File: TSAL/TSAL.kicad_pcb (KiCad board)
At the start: 2 copper layers, 100 x 56 mm, 129 parts, among them IC1 ISO224ADWVR, IC2 ISO224ADWVR, IC3 LTC6995IS6-2#TRMPBF, IC4 LTC6995IS6-2#TRMPBF, J1 Conn_SDC, J2 Conn_TSAL, J3 Conn_AIR, J4 Conn_01x02, J5 Conn_VI, J6 Conn_Control, J7 Conn_HV, J8 Conn_Pre, K1 G2RL-2, Q1 ZXM61N02F, Q2 ZXM61N02F, Q3 ZXM61N02F, Q4 ZXM61N02F, Q5 IXTA6N100D2, U3 TLV7041DBV, U4 TLV7041DBV, U5 74LVC1G08, U6 AP2205-W5-7, U7 AP2205-W5-7, U9 AP2204K-ADJ

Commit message: chore: basic section of layout
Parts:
- removed C11, C13, C18: 0.1u, Capacitor_SMD:C_0603_1608Metric
- removed C12: 0.22u, Capacitor_SMD:C_0603_1608Metric
- removed C14, C15, C19, C33: 1u, Capacitor_SMD:C_0603_1608Metric
- removed IC1, IC2: ISO224ADWVR, Package_SO:SOIC-8_7.5x5.85mm_P1.27mm
- removed RV2, RV4: 10K, Potentiometer_THT:Potentiometer_Bourns_3296W_Vertical
- removed TP3, TP9: TestPoint, TestPoint:TestPoint_THTPad_D1.5mm_Drill0.7mm
- added C1: 330p, Capacitor_SMD:C_0603_1608Metric, F.Cu at (111.0, 104.3)
- added C3: 330p, Capacitor_SMD:C_0603_1608Metric, F.Cu at (111.0, 106.8)
- added C4: 1n, Capacitor_SMD:C_0603_1608Metric, F.Cu at (89.2, 100.9)
- added F2: 0ACJ-2000-TE, BelFuse:0ACJ, F.Cu at (83.0, 71.0)
- added R1: 3k3, Resistor_SMD:R_0603_1608Metric, F.Cu at (111.0, 111.8)
- added R2: 3k3, Resistor_SMD:R_0603_1608Metric, F.Cu at (111.0, 114.3)
- added R3: 3k3, Resistor_SMD:R_0603_1608Metric, F.Cu at (115.0, 104.3)
- added R39: 1M, Resistor_SMD:R_0603_1608Metric, F.Cu at (91.0, 61.4)
- added R4: 3k3, Resistor_SMD:R_0603_1608Metric, F.Cu at (115.0, 106.8)
- added R46: 1M, Resistor_SMD:R_0603_1608Metric, F.Cu at (91.0, 58.2)
- added R47: 1M, Resistor_SMD:R_0603_1608Metric, F.Cu at (91.0, 55.0)
- added R48: 1M, Resistor_SMD:R_0603_1608Metric, F.Cu at (91.0, 51.8)
- added R5: 100k, Resistor_SMD:R_0603_1608Metric, F.Cu at (93.2, 100.9)
- added R7: 1M, Resistor_SMD:R_0603_1608Metric, F.Cu at (93.2, 103.4)
- added TP1: TestPoint, TestPoint:TestPoint_THTPad_D1.5mm_Drill0.7mm, F.Cu at (101.9, 115.9)
- added U1: AMC1351, Package_SO:SOIC-8_7.5x5.85mm_P1.27mm, F.Cu at (107.5, 64.0)
- added U10: TLV7041DBV, Package_TO_SOT_SMD:SOT-23-5, F.Cu at (75.7, 104.4)
- added U2: TLV7041DBV, Package_TO_SOT_SMD:SOT-23-5, F.Cu at (105.3, 109.3)
- added U8: AMC1351, Package_SO:SOIC-8_7.5x5.85mm_P1.27mm, F.Cu at (107.5, 76.5)
- C10: value 1u -> 0.1u
- C20, C22, C23, C34, G***, R40, R41, R42, R43, U6, U9, kibuzzard-6788E0FE: moved to F.Cu
- C5: value 0.22u -> 1u
- C8: value 0.22u -> 1n
- C9: value 0.22u -> 0.1u
- D2: value 1SS355VM -> 1N4148W; footprint Diode_SMD:D_SOD-323F -> Diode_SMD:D_SOD-123
- D3: value BYG10J -> S1J
- J6: value Conn_Control -> Conn_PRE
- J8: value Conn_Pre -> Conn_control
- Q1, Q2, Q3, Q4: value ZXM61N02F -> 2N7002
- Q5: value IXTA6N100D2 -> DN2470K4; footprint Package_TO_SOT_THT:TO-247-3_Vertical -> Package_TO_SOT_SMD:TO-252-2
- R12, R15: value 82K -> 40k
- R13: value 5.1 -> 20k
- R17: value 5.1 -> 37k
- R20: value 1k -> 3k3
- R22, R23, R24: value 1k -> 1M
- moved G*** 57.5 mm to (45.5, 104.8), turned to 0 degrees
- moved kibuzzard-6788E0FE 57.5 mm to (45.5, 116.1), turned to 0 degrees
- moved G*** 38.9 mm to (34.5, 67.5), turned to 0 degrees
- moved C10 32.8 mm to (82.2, 95.6)
- moved C5 32.8 mm to (83.4, 99.6)
- moved C6 32.8 mm to (84.0, 103.7)
- moved C7 32.8 mm to (82.1, 103.7)
- moved C8 32.8 mm to (83.4, 101.2)
- moved C9 32.8 mm to (83.4, 93.2)
- moved C22 31.7 mm to (165.3, 19.8)
- moved G*** 28.2 mm to (43.0, 87.0), turned to 0 degrees
- moved D3 28.0 mm to (71.2, 71.8), turned to 90 degrees
- moved R42 27.4 mm to (162.6, 17.3), turned to 180 degrees
- moved U6 26.7 mm to (162.1, 20.0), turned to 180 degrees
- moved J5 24.8 mm to (92.8, 33.4)
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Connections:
- net BATT+ renamed Net-(D10-A)
- net BATT- renamed Net-(D1-K)
- C5 pad 1: HV- -> +5VA
- C5 pad 2: Net-(IC1-VCAP) -> HV-
- C8 pad 1: Net-(IC1-IN) -> Net-(C8-Pad1)
- C9 pad 1: Net-(IC2-IN) -> +5VA
- D3 pad 1: HV+ -> Net-(D3-K)
- D3 pad 2: HV- -> Net-(D3-A)
- J7 pad 3: unconnected-(J7-Pin_3-Pad3) -> Net-(D3-A)
- R11 pad 2: Net-(IC1-IN) -> Net-(C8-Pad1)
- R12 pad 2: Net-(R12-Pad2) -> Net-(C8-Pad1)
- R13 pad 1: Net-(R12-Pad2) -> Net-(R13-Pad1)
- R13 pad 2: Net-(IC1-IN) -> Net-(U3--)
- R15 pad 2: Net-(R15-Pad2) -> Net-(U10-+)
- R17 pad 1: Net-(R15-Pad2) -> Net-(U10--)
- R17 pad 2: Net-(IC2-IN) -> HV-
- R19 pad 2: Net-(IC2-IN) -> Net-(U10-+)
- R20 pad 1: Net-(U3-+) -> Net-(R20-Pad1)
- R20 pad 2: Net-(IC1-OUTP) -> Net-(U4-+)
- R22 pad 2: Net-(R21-Pad2) -> Net-(U4--)
- R23 pad 1: +5V -> Net-(R23-Pad1)
- R23 pad 2: Net-(R23-Pad2) -> Net-(U4--)
- R24 pad 1: Net-(U4-+) -> GND2
- R24 pad 2: Net-(IC2-OUTP) -> Net-(R23-Pad1)
- TP8 pad 1: Net-(R23-Pad2) -> Net-(TP8-Pad1)
- U4 pad 1: Net-(R23-Pad2) -> Net-(TP8-Pad1)
- U5 pad 1: Net-(R23-Pad2) -> Net-(TP8-Pad1)
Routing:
- net +5V: track 172.0 -> 0.00 mm, vias 5 -> 0
- net HV-: track 163.0 -> 0.00 mm, vias 2 -> 0
- net /SDC: track 71.5 -> 0.00 mm
- net Net-(D6-K): track 56.2 -> 0.00 mm
- net HV+: track 52.4 -> 0.00 mm
- net VCC: track 49.8 -> 0.00 mm
- net +5VA: track 48.8 -> 0.00 mm, vias 3 -> 0
- net Net-(IC4-RST/~{RST}): track 43.2 -> 0.00 mm, vias 1 -> 0
- net Net-(J5-Pin_1): track 42.9 -> 0.00 mm
- net Net-(IC3-OUT): track 39.6 -> 0.00 mm, vias 2 -> 0
- net Net-(J6-Pin_1): track 29.0 -> 0.00 mm
- net Net-(IC3-RST/~{RST}): track 26.5 -> 0.00 mm, vias 1 -> 0
- net Net-(PS1-+VOUT): track 26.4 -> 0.00 mm
- net Net-(IC1-IN): track 25.8 -> 0.00 mm, vias 2 -> 0
- net Net-(D9-K): track 24.7 -> 0.00 mm
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- removed copper zone on B.Cu, net GND2
- removed copper zone on F.Cu, net GND2
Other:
- outline, holes or cut-outs redrawn
- board text added: "NCKU Formula Racing TSAL & PreCharge Rev. 2025.04"
- board text removed: "-"
- board text removed: "LV"
- board text removed: "NCKU Formula Racing TSAL & PreCharge Rev. 2025.02"

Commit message: Add files via upload
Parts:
- G*** (x2), R13, R5, R7, kibuzzard-6788E0FE: moved to B.Cu
- moved G*** 66.7 mm to (99.3, 83.2)
- moved G*** 61.1 mm to (98.2, 60.9), turned to 180 degrees
- moved G*** 56.3 mm to (79.3, 59.8), turned to 180 degrees
- moved kibuzzard-6788E0FE 56.3 mm to (79.3, 71.0), turned to 180 degrees
- moved R42 48.7 mm to (118.1, 36.9)
- moved U6 48.7 mm to (117.6, 39.6)
- moved C22 48.7 mm to (120.7, 39.4)
- moved C23 48.7 mm to (114.2, 39.6)
- moved R43 48.7 mm to (114.7, 36.9)
- moved R7 48.4 mm to (125.1, 67.1)
- moved R13 47.5 mm to (127.7, 68.1), turned to 90 degrees
- moved R5 45.0 mm to (125.1, 69.2)
- moved C20 42.9 mm to (132.8, 45.7)
- moved C34 42.9 mm to (126.4, 45.5)
- moved R41 42.9 mm to (129.1, 42.8)
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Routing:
- net GND2: track 0.00 -> 340.3 mm, vias 0 -> 5
- net +5V: track 0.00 -> 176.5 mm, vias 0 -> 3
- net HV-: track 0.00 -> 138.8 mm, vias 0 -> 4
- net /SDC: track 0.00 -> 104.0 mm
- net Net-(D6-K): track 0.00 -> 82.3 mm
- net VCC: track 0.00 -> 63.4 mm
- net +5VA: track 0.00 -> 54.5 mm, vias 0 -> 4
- net Net-(IC3-RST/~{RST}): track 0.00 -> 54.0 mm, vias 0 -> 2
- net HV+: track 0.00 -> 53.7 mm
- net Net-(IC4-RST/~{RST}): track 0.00 -> 52.1 mm, vias 0 -> 4
- net Net-(IC3-OUT): track 0.00 -> 50.5 mm, vias 0 -> 2
- net Net-(U4--): track 0.00 -> 46.8 mm, vias 0 -> 1
- net Net-(U3-+): track 0.00 -> 42.5 mm, vias 0 -> 2
- net Net-(R2-Pad1): track 0.00 -> 40.5 mm, vias 0 -> 2
- net Net-(PS1-+VOUT): track 0.00 -> 37.9 mm
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- added copper zone on B.Cu, net GND2
- added copper zone on F.Cu, net GND2

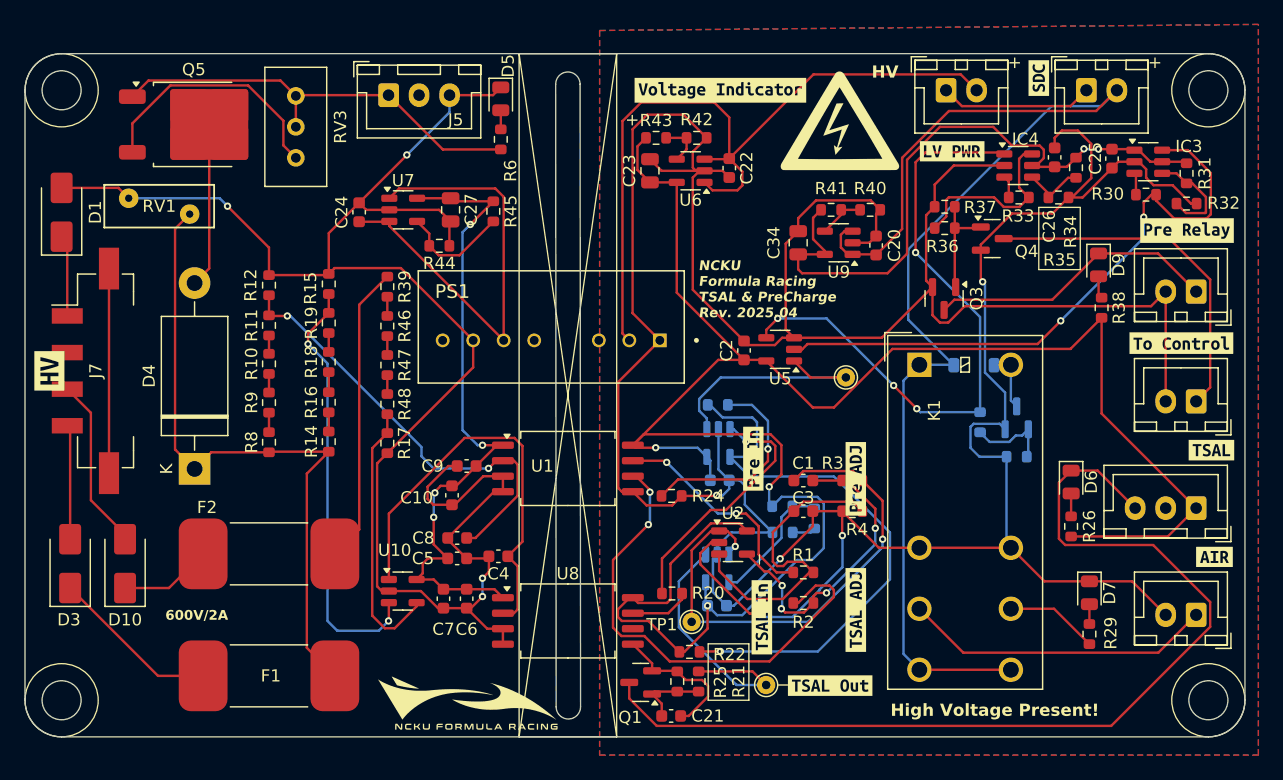
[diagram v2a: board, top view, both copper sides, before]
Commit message: fix: optimize VI schematics
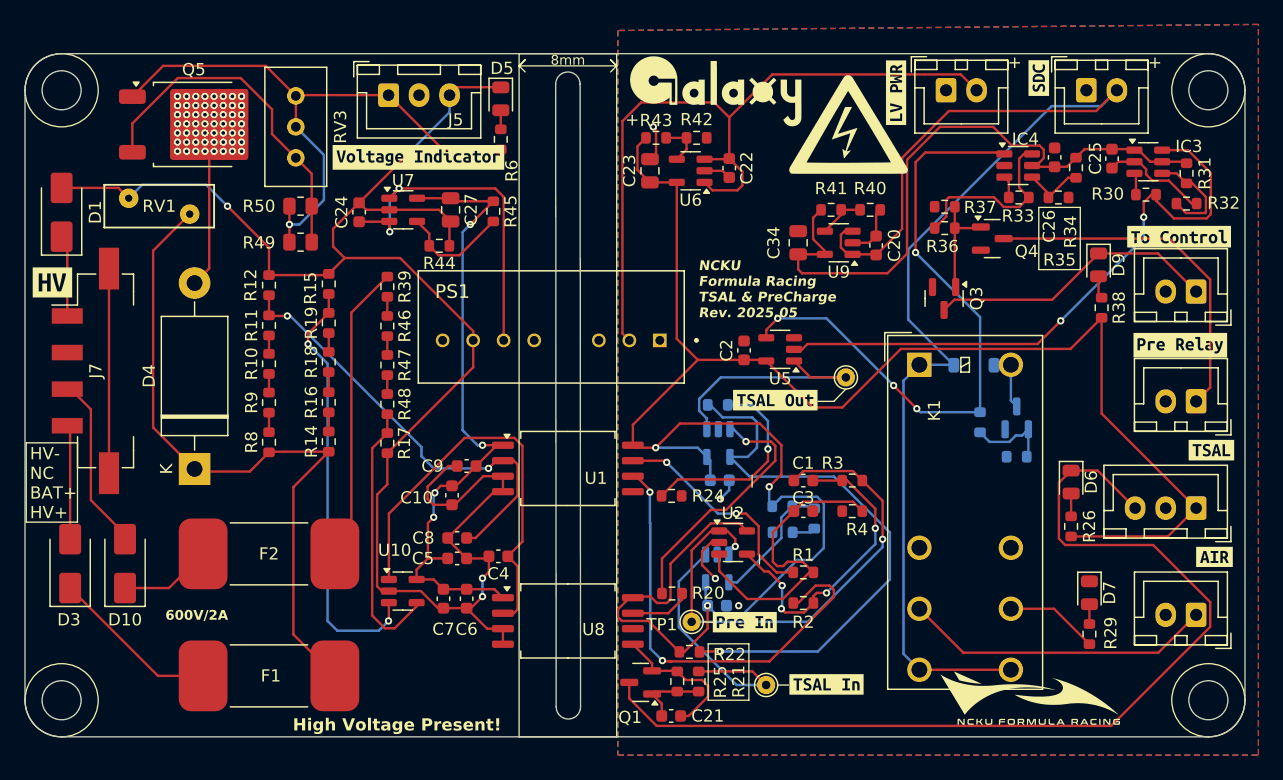
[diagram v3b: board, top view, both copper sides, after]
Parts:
- removed kibuzzard-67893696: G***, kibuzzard-67893696
- removed kibuzzard-678936A8: G***, kibuzzard-678936A8
- added R49: 1k, Resistor_SMD:R_0805_2012Metric, F.Cu at (85.6, 45.5)
- added R50: 1k, Resistor_SMD:R_0805_2012Metric, F.Cu at (85.6, 42.5)
- G***: moved to F.Cu
- moved G*** 46.1 mm to (145.4, 82.8)
- moved G*** 35.1 mm to (119.7, 33.1), turned to 0 degrees
- moved kibuzzard-67879B82 25.4 mm to (95.2, 38.5)
- moved kibuzzard-67A05267 23.8 mm to (124.5, 58.4)
- moved kibuzzard-67A0528E 13.4 mm to (122.0, 76.6), turned to 0 degrees
- moved kibuzzard-6787964A 9.42 mm to (157.7, 53.9)
- moved kibuzzard-67872F86 8.73 mm to (157.6, 45.0)
- moved kibuzzard-67A052A1 7.64 mm to (128.7, 81.7), turned to 0 degrees
- moved kibuzzard-67888934 7.25 mm to (65.2, 48.8), turned to 0 degrees
- moved kibuzzard-67872213 6.65 mm to (134.4, 33.2), turned to 90 degrees
- moved G*** 0.76 mm to (130.5, 35.8)
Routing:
- net GND2: track 340.3 -> 36.4 mm, vias 5 -> 4
- net Net-(J5-Pin_1): track 35.7 -> 50.2 mm, vias 0 -> 1
- net Net-(PS1-+VOUT): track 37.9 -> 29.0 mm, vias 0 -> 2
- net Net-(Q5-S): track 20.7 -> 28.6 mm
- net Net-(R2-Pad1): track 40.5 -> 37.3 mm
- net HV+: track 53.7 -> 56.3 mm
- net +5V: track 176.5 -> 175.0 mm
- net HV-: track 138.8 -> 140.3 mm
- net VCC: track 63.4 -> 62.0 mm
- net Net-(IC3-RST/~{RST}): track 54.0 -> 53.9 mm, vias 2 -> 0
- net Net-(D4-A): vias 0 -> 56
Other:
- board text added: "8mm"
- board text added: "HV- NC BAT+ HV+"
- board text added: "NCKU Formula Racing TSAL & PreCharge Rev. 2025.05"
- board text removed: "HV"
- board text removed: "NCKU Formula Racing TSAL & PreCharge Rev. 2025.04"

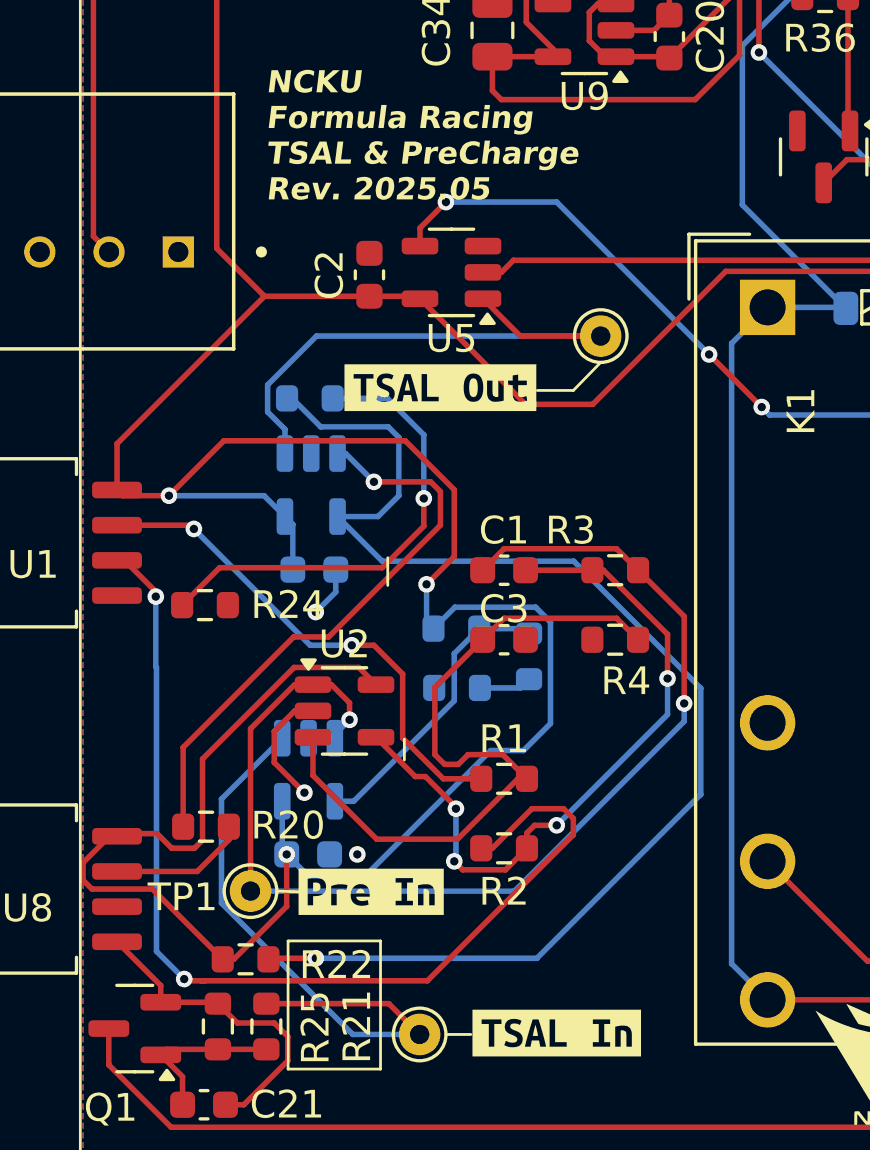
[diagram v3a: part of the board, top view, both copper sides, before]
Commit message: change comparator
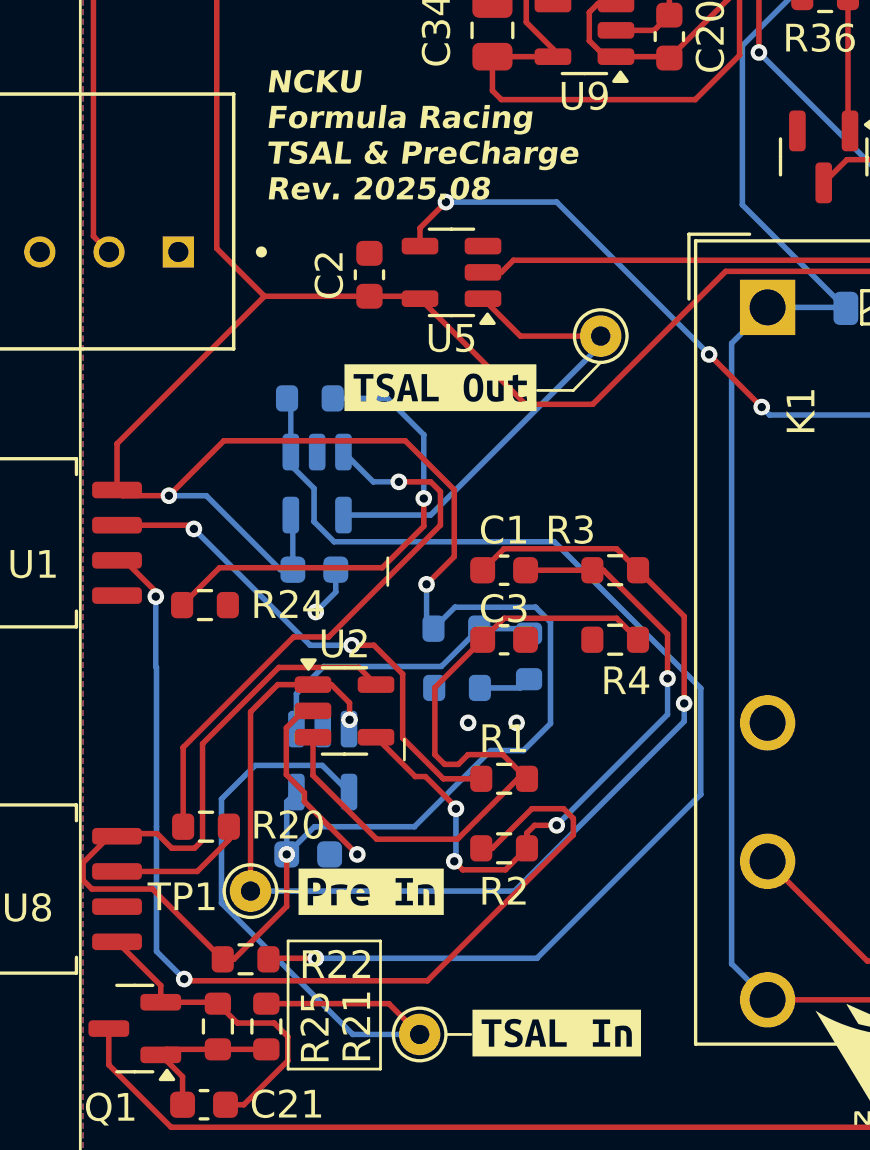
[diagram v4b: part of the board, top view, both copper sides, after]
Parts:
- U3, U4: value TLV7041DBV -> AS331KTR-G1
- moved U3 0.61 mm to (120.2, 71.9)
- moved U4 0.22 mm to (120.0, 61.9)
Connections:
- U3 pad 1: Net-(R21-Pad2) -> Net-(U3--)
- U3 pad 4: Net-(U3--) -> Net-(R21-Pad2)
- U4 pad 1: Net-(TP8-Pad1) -> Net-(U4--)
- U4 pad 4: Net-(U4--) -> Net-(TP8-Pad1)
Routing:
- net Net-(U4--): track 46.8 -> 43.4 mm
- net Net-(TP8-Pad1): track 20.3 -> 17.0 mm
- net GND2: track 36.4 -> 38.9 mm, vias 4 -> 5
- net Net-(R21-Pad2): track 22.0 -> 24.4 mm
- net +5V: track 175.0 -> 176.3 mm
- net Net-(U3-+): track 42.5 -> 41.9 mm
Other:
- board text added: "NCKU Formula Racing TSAL & PreCharge Rev. 2025.08"
- board text removed: "NCKU Formula Racing TSAL & PreCharge Rev. 2025.05"
